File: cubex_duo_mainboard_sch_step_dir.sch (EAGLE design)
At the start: 7 parts, among them IC1 PIC32MX440F256H, IC2 A3979, IC3 A3979, IC4 A3979

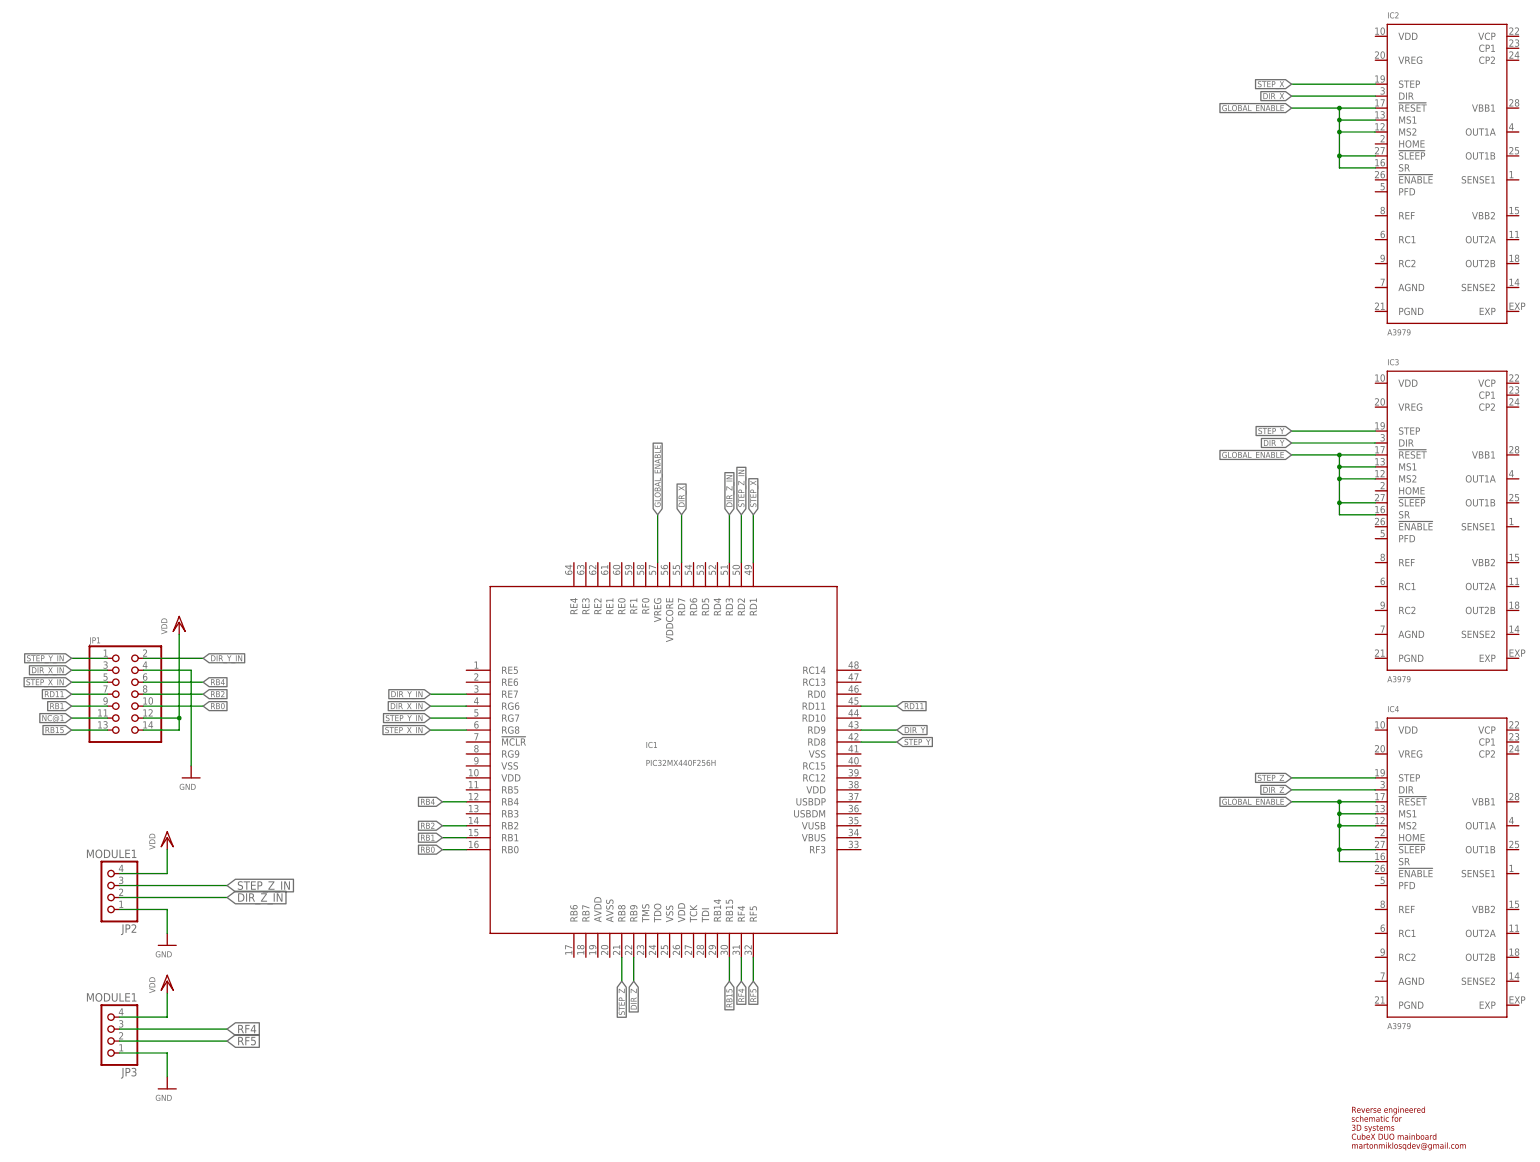
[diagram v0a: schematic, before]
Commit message: Add nENABLE to the step dir sch.
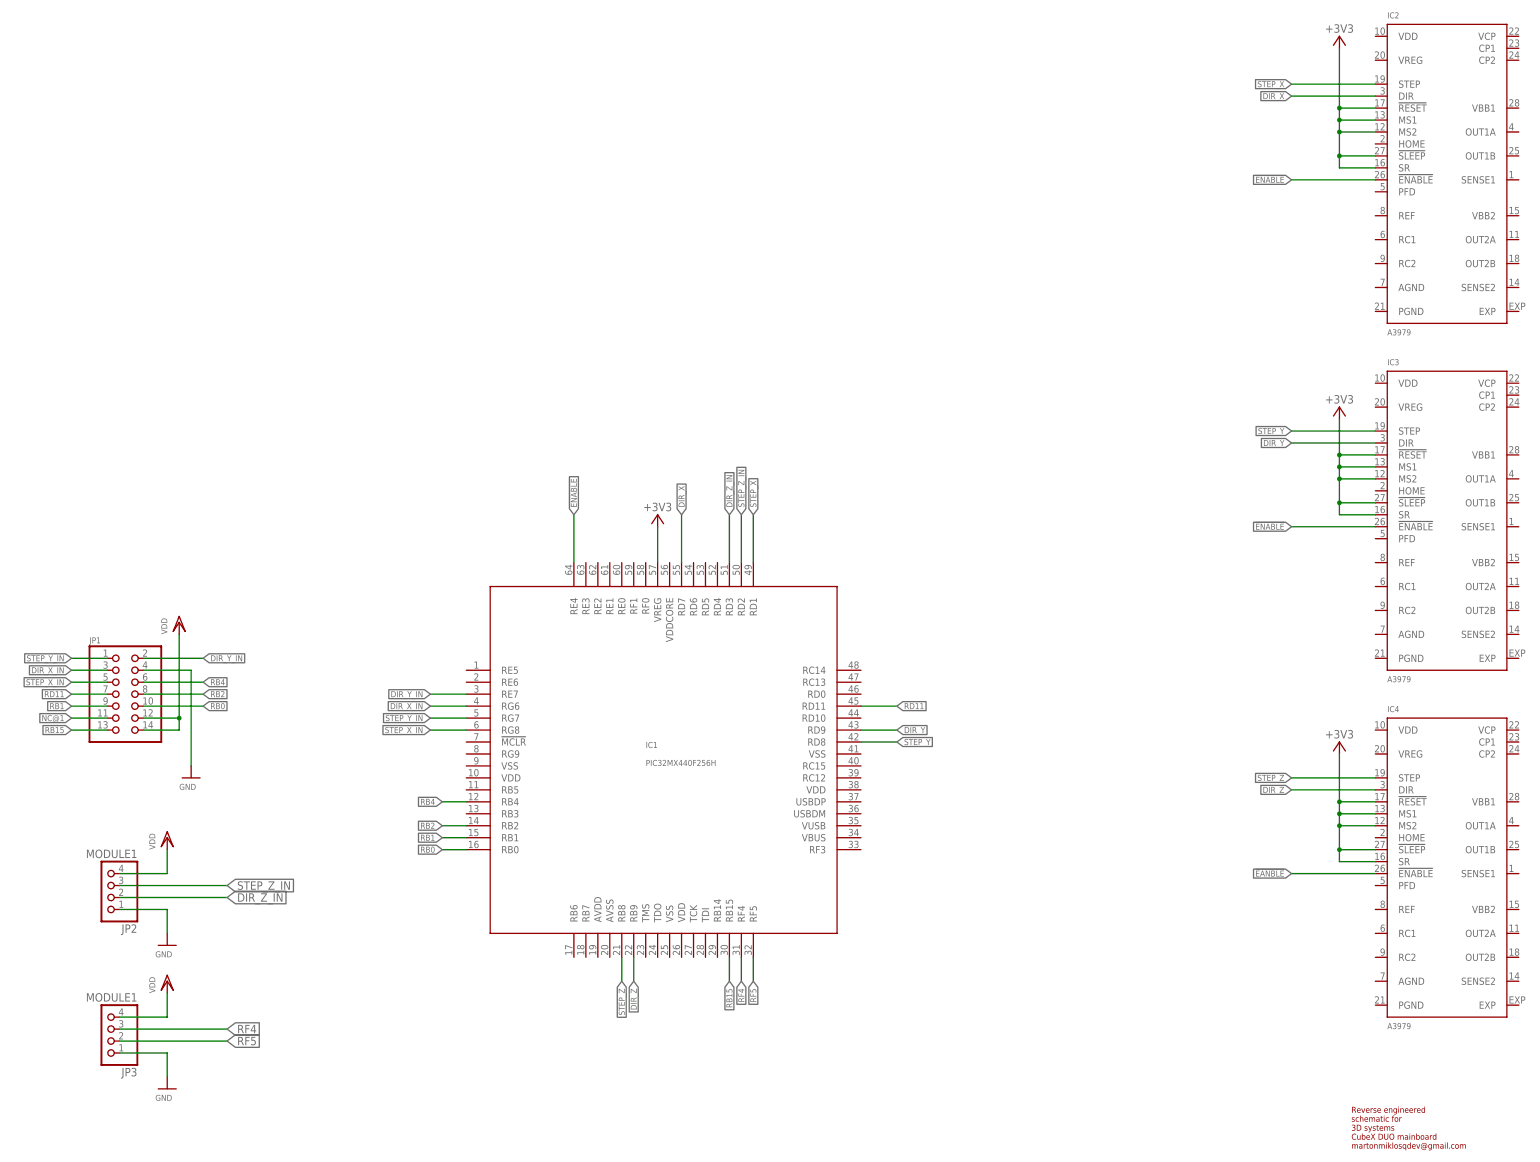
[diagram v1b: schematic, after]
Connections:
- net GLOBAL_ENABLE renamed +3V3
- new net !EANBLE: IC4.!ENABLE
- new net !ENABLE: IC1.RE4, IC2.!ENABLE, IC3.!ENABLE
